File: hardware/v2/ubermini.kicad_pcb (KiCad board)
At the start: 4 copper layers, 49.8 x 33.9 mm, 73 parts, among them J1 USB_OTG, P1 SMA-CONN, P2 sma, P3 sma, P4 uart1, P5 SWD, P6 boot, P7 sma, SW1 SW_PUSH, U1 CC2591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

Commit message: hw update
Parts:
- J1: footprint Connect:USB_Mini-B -> v2:USB_Mini-B_s
- moved D6 78.5 mm to (80.2, 68.5), turned to 90 degrees
- moved R15 76.7 mm to (76.9, 69.5), turned to 180 degrees
- moved R6 64.0 mm to (104.9, 60.6)
- moved R7 64.0 mm to (106.3, 60.6)
- moved U3 63.7 mm to (85.3, 50.5)
- moved C1 63.6 mm to (106.8, 56.2)
- moved C25 63.6 mm to (89.8, 61.8)
- moved P6 63.6 mm to (107.8, 42.2)
- moved R8 63.6 mm to (92.8, 44.8)
- moved SW1 63.6 mm to (110.3, 57.6)
- moved U2 63.6 mm to (98.5, 51.5)
- moved BT1 63.6 mm to (65.9, 66.9)
- moved C10 63.6 mm to (75.0, 56.5)
- moved C11 63.6 mm to (73.5, 56.5)
- moved C14 63.6 mm to (79.0, 46.9)
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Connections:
- U2 pad 1: (no net) -> Net-(U2-Pad1)
- U2 pad 14: (no net) -> Net-(U2-Pad14)
- U2 pad 15: (no net) -> Net-(U2-Pad15)
- U2 pad 16: (no net) -> Net-(U2-Pad16)
- U2 pad 17: (no net) -> Net-(U2-Pad17)
- U2 pad 2: (no net) -> /EN
- U2 pad 20: (no net) -> Net-(U2-Pad20)
- U2 pad 24: (no net) -> Net-(U2-Pad24)
- U2 pad 25: (no net) -> Net-(U2-Pad25)
- U2 pad 26: (no net) -> Net-(U2-Pad26)
- U2 pad 27: (no net) -> Net-(U2-Pad27)
- U2 pad 29: (no net) -> Net-(U2-Pad29)
- U2 pad 3: /EN -> /HGM
- U2 pad 30: (no net) -> Net-(U2-Pad30)
- U2 pad 33: (no net) -> Net-(U2-Pad33)
- U2 pad 34: (no net) -> Net-(U2-Pad34)
- U2 pad 35: (no net) -> Net-(U2-Pad35)
- U2 pad 36: (no net) -> Net-(U2-Pad36)
- U2 pad 37: (no net) -> Net-(U2-Pad37)
- U2 pad 38: (no net) -> Net-(U2-Pad38)
- U2 pad 39: (no net) -> Net-(U2-Pad39)
- U2 pad 4: /HGM -> /SPI1_CS
- U2 pad 40: (no net) -> Net-(U2-Pad40)
- U2 pad 41: (no net) -> Net-(U2-Pad41)
- U2 pad 6: (no net) -> Net-(U2-Pad6)
- U2 pad 62: (no net) -> Net-(U2-Pad62)
- U3 pad 11: (no net) -> Net-(U3-Pad11)
- U3 pad 12: (no net) -> Net-(U3-Pad12)
- U3 pad 13: (no net) -> Net-(U3-Pad13)
- U3 pad 36: (no net) -> Net-(U3-Pad36)
- U3 pad 37: (no net) -> Net-(U3-Pad37)
- U3 pad 38: (no net) -> Net-(U3-Pad38)
- U3 pad 39: (no net) -> Net-(U3-Pad39)
- U3 pad 40: (no net) -> Net-(U3-Pad40)
- U4 pad 2: (no net) -> Net-(U4-Pad2)
- U4 pad 9: (no net) -> Net-(U4-Pad9)
- U5 pad 1: (no net) -> /SPI1_CS
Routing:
- net GND: track 441.9 -> 661.2 mm, vias 40 -> 109
- net /SPI1_MO: track 5.65 -> 36.1 mm, vias 1 -> 2
- net +3V3: track 72.5 -> 102.1 mm, vias 7 -> 9
- net /SPI1_SCK: track 3.86 -> 32.4 mm, vias 1 -> 2
- net +1V8: track 71.1 -> 98.7 mm, vias 6 -> 11
- net /SPI1_MI: track 4.69 -> 30.0 mm, vias 1 -> 2
- net /SPI1_CS: track 0.00 -> 23.0 mm, vias 0 -> 2
- net +3.3VA: track 73.7 -> 86.2 mm, vias 6 -> 9
- net /VBUS: track 50.1 -> 54.1 mm
- net /HGM: track 36.1 -> 32.4 mm
- net Net-(D6-Pad1): track 0.00 -> 2.20 mm
- net Net-(R7-Pad2): track 19.6 -> 18.5 mm
- net /EN: track 31.6 -> 32.6 mm
- net Net-(R6-Pad2): track 18.2 -> 17.3 mm
- net Net-(C19-Pad2): track 9.06 -> 9.92 mm
- added copper zone on POW.Cu, net +1V8
- added copper zone on POW.Cu, net +3.3VA
- added copper zone on POW.Cu, net +3V3
- added copper zone on B.Cu, net GND
- added copper zone on F.Cu, net GND
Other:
- board text added: "GND"
- board text added: "POWER"

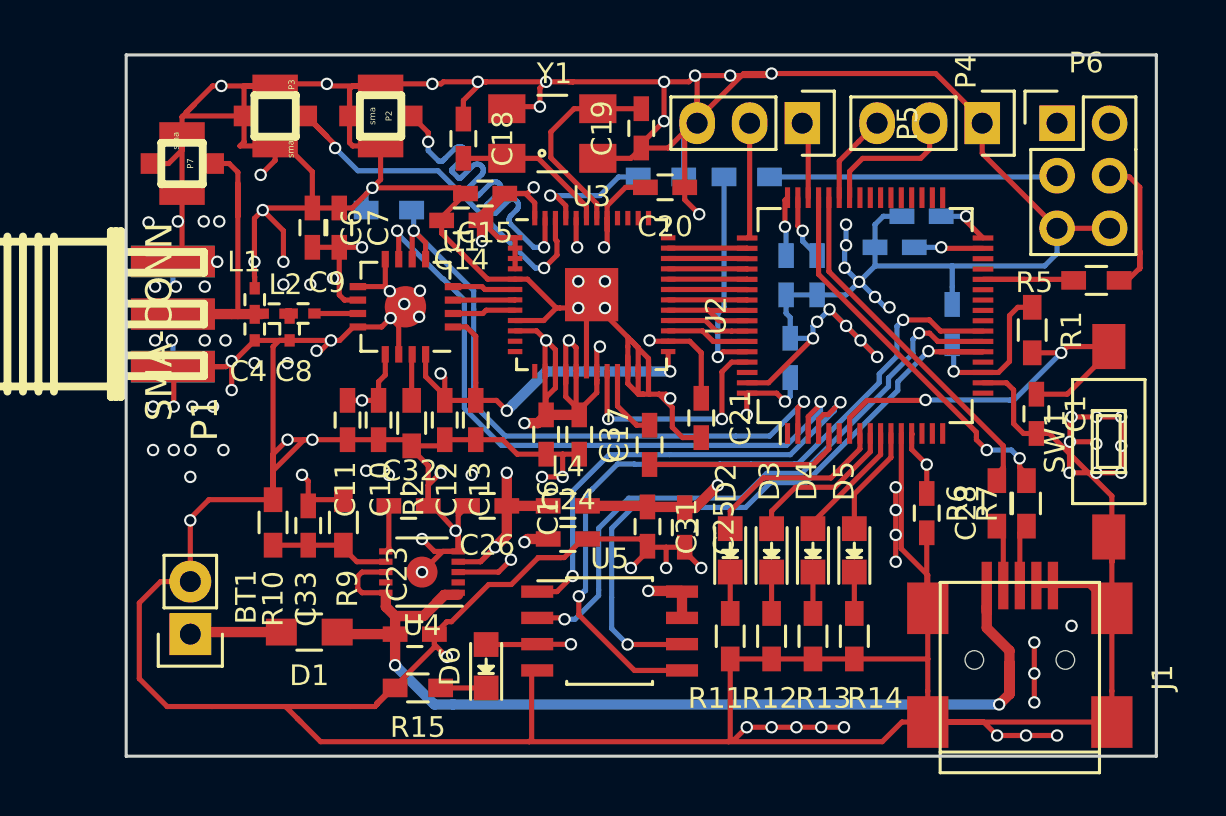
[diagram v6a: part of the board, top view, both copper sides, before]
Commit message: add logo
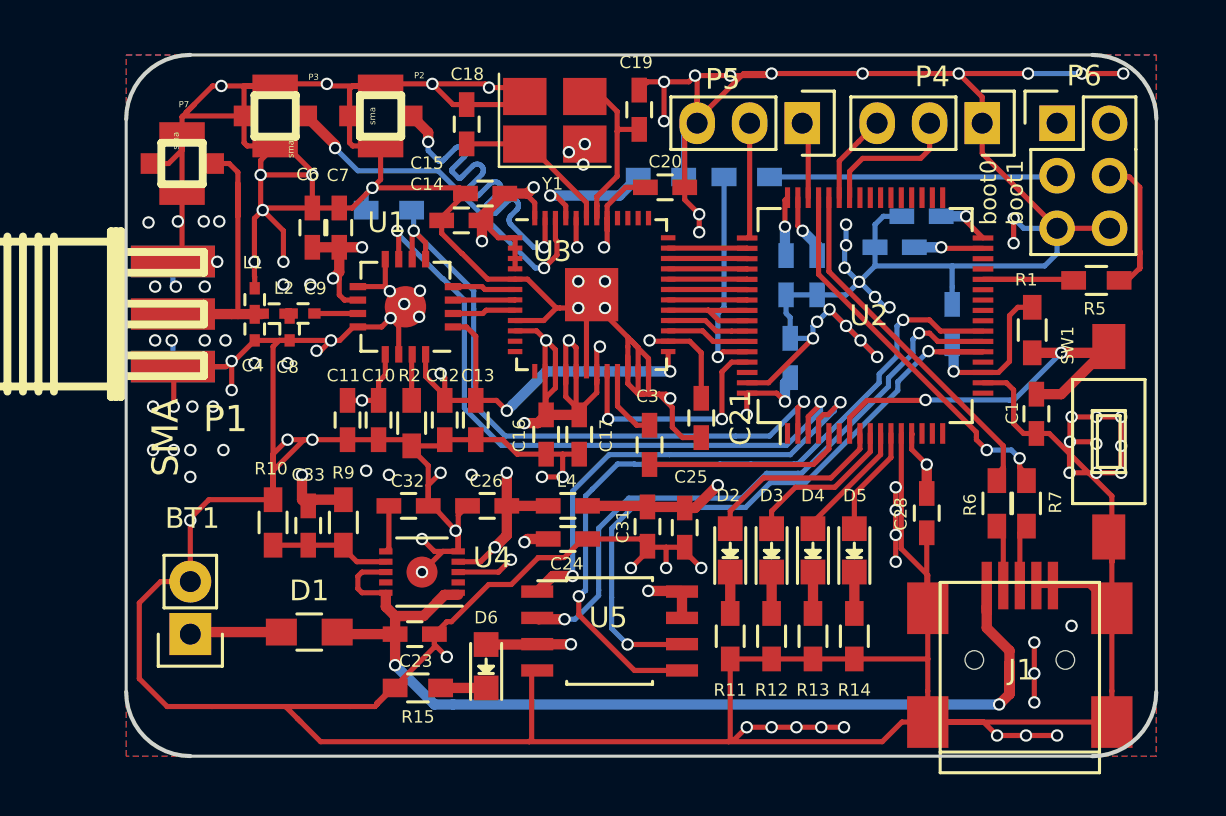
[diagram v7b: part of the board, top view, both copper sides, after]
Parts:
- added ?: Symbol_OSHW-Logo_SilkScreen_BIG, Symbols:Symbol_OSHW-Logo_SilkScreen_BIG, B.Cu at (75.6, 39.0)
- added ?: LOGO, v2:kg_logo, B.Cu at (97.6, 60.9)
- P1: value SMA-CONN -> SMA
- Y1: footprint Crystals:Crystal_SMD_0603_4Pads -> v2:3225
- moved C19 0.91 mm to (87.6, 41.5), turned to 270 degrees
- moved C18 0.72 mm to (79.3, 42.2)
- moved Y1 0.65 mm to (83.5, 42.1)
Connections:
- U2 pad 1: Net-(U2-Pad1) -> (no net)
- U2 pad 14: Net-(U2-Pad14) -> (no net)
- U2 pad 15: Net-(U2-Pad15) -> (no net)
- U2 pad 16: Net-(U2-Pad16) -> (no net)
- U2 pad 17: Net-(U2-Pad17) -> (no net)
- U2 pad 20: Net-(U2-Pad20) -> (no net)
- U2 pad 24: Net-(U2-Pad24) -> (no net)
- U2 pad 25: Net-(U2-Pad25) -> (no net)
- U2 pad 26: Net-(U2-Pad26) -> (no net)
- U2 pad 27: Net-(U2-Pad27) -> (no net)
- U2 pad 29: Net-(U2-Pad29) -> (no net)
- U2 pad 30: Net-(U2-Pad30) -> (no net)
- U2 pad 33: Net-(U2-Pad33) -> (no net)
- U2 pad 34: Net-(U2-Pad34) -> (no net)
- U2 pad 35: Net-(U2-Pad35) -> (no net)
- U2 pad 36: Net-(U2-Pad36) -> (no net)
- U2 pad 37: Net-(U2-Pad37) -> (no net)
- U2 pad 38: Net-(U2-Pad38) -> (no net)
- U2 pad 39: Net-(U2-Pad39) -> (no net)
- U2 pad 40: Net-(U2-Pad40) -> (no net)
- U2 pad 41: Net-(U2-Pad41) -> (no net)
- U2 pad 6: Net-(U2-Pad6) -> (no net)
- U2 pad 62: Net-(U2-Pad62) -> (no net)
- U3 pad 11: Net-(U3-Pad11) -> (no net)
- U3 pad 12: Net-(U3-Pad12) -> (no net)
- U3 pad 13: Net-(U3-Pad13) -> (no net)
- U3 pad 36: Net-(U3-Pad36) -> (no net)
- U3 pad 37: Net-(U3-Pad37) -> (no net)
- U3 pad 38: Net-(U3-Pad38) -> (no net)
- U3 pad 39: Net-(U3-Pad39) -> (no net)
- U3 pad 40: Net-(U3-Pad40) -> (no net)
- U4 pad 2: Net-(U4-Pad2) -> (no net)
- U4 pad 9: Net-(U4-Pad9) -> (no net)
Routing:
- net GND: track 661.2 -> 668.5 mm, vias 109 -> 119
- net +3.3VA: track 86.2 -> 90.3 mm
- added copper zone on GND.Cu, net GND
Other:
- outline, holes or cut-outs redrawn
- board text added: "boot0 boot1"

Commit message: fix hw
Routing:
- net +1V8: track 98.7 -> 104.3 mm
- net GND: track 668.5 -> 666.5 mm, vias 119 -> 118
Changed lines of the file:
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@@
     (thickness 1.6)
     (drawings 22)
-    (tracks 1368)
+    (tracks 1379)
     (zones 0)
     (modules 75)
@@
     (pad_to_mask_clearance 0.2)
     (aux_axis_origin 62.8 38.9)
-    (grid_origin 62.8 38.9)
     (visible_elements 7FFFEFFF)
     (pcbplotparams
@@
   (segment (start 106.18 47.28) (end 105.7 46.8) (width 0.25) (layer B.Cu) (net 2))
   (via (at 105.7 46.8) (size 0.6) (drill 0.4) (layers F.Cu B.Cu) (net 2))
-  (segment (start 109 39.8) (end 111 39.8) (width 0.25) (layer F.Cu) (net 2))
-  (via (at 111 39.8) (size 0.6) (drill 0.4) (layers F.Cu B.Cu) (net 2))
   (segment (start 106.4 39.8) (end 109 39.8) (width 0.25) (layer B.Cu) (net 2))
   (via (at 109 39.8) (size 0.6) (drill 0.4) (layers F.Cu B.Cu) (net 2))
@@
   (segment (start 86.55 55.875) (end 87.475 56.8) (width 0.25) (layer F.Cu) (net 6))
   (segment (start 87.475 56.8) (end 88.1 56.8) (width 0.25) (layer F.Cu) (net 6))
+  (segment (start 67.00114 44.15034) (end 67.77692 44.15034) (width 0.25) (layer F.Cu) (net 7))
   (segment (start 68.2 51.427) (end 68.2 46.7) (width 0.25) (layer F.Cu) (net 7))
   (segment (start 68.2 46.7) (end 68.2 45.1) (width 0.25) (layer F.Cu) (net 7))
-  (segment (start 67.00114 44.15034) (end 67.77692 44.15034) (width 0.25) (layer F.Cu) (net 7))
   (segment (start 67.77692 44.15034) (end 68.2 44.57342) (width 0.25) (layer F.Cu) (net 7))
   (segment (start 68.2 44.57342) (end 68.2 46.7) (width 0.25) (layer F.Cu) (net 7))
@@
   (segment (start 70.792 51.408) (end 70.8 51.4) (width 0.25) (layer F.Cu) (net 10))
   (segment (start 74 51.4) (end 71.9 51.4) (width 0.25) (layer F.Cu) (net 11))
+  (segment (start 80.54 48.43) (end 80.46 48.51) (width 0.5) (layer F.Cu) (net 12))
+  (segment (start 80.54 48.02) (end 80.54 48.43) (width 0.5) (layer F.Cu) (net 12))
+  (segment (start 80.360001 48.199999) (end 80.54 48.02) (width 0.5) (layer F.Cu) (net 12))
+  (segment (start 80 47.9) (end 80.299999 48.199999) (width 0.5) (layer F.Cu) (net 12))
+  (segment (start 80.299999 48.199999) (end 80.360001 48.199999) (width 0.5) (layer F.Cu) (net 12))
+  (segment (start 81.6 47.74) (end 80.16 47.74) (width 0.25) (layer F.Cu) (net 12))
+  (segment (start 80.16 47.74) (end 80 47.9) (width 0.25) (layer F.Cu) (net 12))
+  (segment (start 81.6 48.24) (end 80.34 48.24) (width 0.25) (layer F.Cu) (net 12))
+  (segment (start 80.34 48.24) (end 80 47.9) (width 0.25) (layer F.Cu) (net 12))
+  (segment (start 80 47.9) (end 80.84 48.74) (width 0.25) (layer F.Cu) (net 12))
+  (segment (start 80.84 48.74) (end 81.6 48.74) (width 0.25) (layer F.Cu) (net 12))
+  (segment (start 81.6 49.24) (end 81.375 49.24) (width 0.25) (layer F.Cu) (net 12))
+  (segment (start 80 48.41) (end 80 47.9) (width 0.25) (layer F.Cu) (net 12))
+  (segment (start 81.375 49.24) (end 81.365 49.23) (width 0.25) (layer F.Cu) (net 12))
+  (segment (start 81.365 49.23) (end 80.85 49.23) (width 0.25) (layer F.Cu) (net 12))
+  (segment (start 80.85 49.23) (end 80.48 48.86) (width 0.25) (layer F.Cu) (net 12))
+  (segment (start 80.48 48.86) (end 80.45 48.86) (width 0.25) (layer F.Cu) (net 12))
+  (segment (start 80.45 48.86) (end 80 48.41) (width 0.25) (layer F.Cu) (net 12))
   (segment (start 81.1 45.6) (end 82.2 45.6) (width 0.5) (layer F.Cu) (net 12))
   (segment (start 82.2 45.6) (end 82.5 45.3) (width 0.5) (layer F.Cu) (net 12))
@@
   (via (at 88.1 52.7) (size 0.6) (drill 0.4) (layers F.Cu B.Cu) (net 12))
   (via (at 80 47.9) (size 0.6) (drill 0.4) (layers F.Cu B.Cu) (net 12))
-  (segment (start 81.6 48.24) (end 81.6 47.74) (width 0.25) (layer F.Cu) (net 12))
-  (segment (start 81.6 48.74) (end 81.6 48.24) (width 0.25) (layer F.Cu) (net 12))
-  (segment (start 81.6 49.24) (end 81.6 48.74) (width 0.25) (layer F.Cu) (net 12))
   (segment (start 82.05 53.4) (end 82.05 51.2) (width 0.25) (layer POW.Cu) (net 12))
   (segment (start 82.05 55.95) (end 82.05 53.4) (width 0.25) (layer POW.Cu) (net 12))
@@
   (segment (start 82.075 62.475) (end 82.05 62.45) (width 0.25) (layer F.Cu) (net 12))
   (via (at 82.05 62.45) (size 0.6) (drill 0.4) (layers F.Cu B.Cu) (net 12))
-  (segment (start 81.6 47.74) (end 80.79 47.74) (width 0.25) (layer F.Cu) (net 12))
-  (segment (start 80.79 47.74) (end 79.95 46.9) (width 0.25) (layer F.Cu) (net 12))
   (segment (start 90.6 55.5) (end 90.6 53.3) (width 0.25) (layer F.Cu) (net 12))
   (segment (start 90.6 53.3) (end 90.04 52.74) (width 0.25) (layer F.Cu) (net 12))
